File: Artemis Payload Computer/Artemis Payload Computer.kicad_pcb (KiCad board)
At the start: 2 copper layers, 11 parts, among them J1 Screw_Terminal_01x02, J2 Screw_Terminal_01x02, U1 HX711, U301 Teensy3.2, U401 FXOS8700+FXAS21002, U501 BMP280, U601 MIC39100-5.0WS

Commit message: Shit
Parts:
- removed U401: FXOS8700+FXAS21002, Artemis Payload Computer:IMU
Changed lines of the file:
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@@
     (tracks 0)
     (zones 0)
-    (modules 11)
-    (nets 67)
+    (modules 10)
+    (nets 57)
   )
   (page A4)
@@
   (net 48 "Net-(U301-Pad18)")
   (net 49 "Net-(U301-Pad17)")
-  (net 50 "Net-(U401-Pad10)")
-  (net 51 "Net-(U401-Pad9)")
-  (net 52 "Net-(U401-Pad8)")
-  (net 53 "Net-(U401-Pad7)")
-  (net 54 "Net-(U401-Pad6)")
-  (net 55 "Net-(U401-Pad5)")
-  (net 56 "Net-(U401-Pad4)")
-  (net 57 "Net-(U401-Pad3)")
-  (net 58 "Net-(U401-Pad2)")
-  (net 59 "Net-(U401-Pad1)")
-  (net 60 "Net-(U501-Pad7)")
-  (net 61 "Net-(U501-Pad6)")
-  (net 62 "Net-(U501-Pad5)")
-  (net 63 "Net-(U501-Pad4)")
-  (net 64 "Net-(U501-Pad3)")
-  (net 65 "Net-(U501-Pad2)")
-  (net 66 "Net-(U501-Pad1)")
+  (net 50 "Net-(U501-Pad7)")
+  (net 51 "Net-(U501-Pad6)")
+  (net 52 "Net-(U501-Pad5)")
+  (net 53 "Net-(U501-Pad4)")
+  (net 54 "Net-(U501-Pad3)")
+  (net 55 "Net-(U501-Pad2)")
+  (net 56 "Net-(U501-Pad1)")
   (net_class Default "This is the default net class."
     (clearance 0.2)
@@
     (add_net "Net-(U301-Pad8)")
     (add_net "Net-(U301-Pad9)")
-    (add_net "Net-(U401-Pad1)")
-    (add_net "Net-(U401-Pad10)")
-    (add_net "Net-(U401-Pad2)")
-    (add_net "Net-(U401-Pad3)")
-    (add_net "Net-(U401-Pad4)")
-    (add_net "Net-(U401-Pad5)")
-    (add_net "Net-(U401-Pad6)")
-    (add_net "Net-(U401-Pad7)")
-    (add_net "Net-(U401-Pad8)")
-    (add_net "Net-(U401-Pad9)")
     (add_net "Net-(U501-Pad1)")
     (add_net "Net-(U501-Pad2)")
@@
     (fp_line (start 16.24 2) (end -1 2) (layer F.SilkS) (width 0.12))
     (pad 7 thru_hole circle (at 15.24 0) (size 1.75 1.75) (drill 1.15) (layers *.Cu *.Mask)
-      (net 60 "Net-(U501-Pad7)"))
+      (net 50 "Net-(U501-Pad7)"))
     (pad 6 thru_hole circle (at 12.7 0) (size 1.75 1.75) (drill 1.15) (layers *.Cu *.Mask)
-      (net 61 "Net-(U501-Pad6)"))
+      (net 51 "Net-(U501-Pad6)"))
     (pad 5 thru_hole circle (at 10.16 0) (size 1.75 1.75) (drill 1.15) (layers *.Cu *.Mask)
-      (net 62 "Net-(U501-Pad5)"))
+      (net 52 "Net-(U501-Pad5)"))
     (pad 4 thru_hole circle (at 7.62 0) (size 1.75 1.75) (drill 1.15) (layers *.Cu *.Mask)
-      (net 63 "Net-(U501-Pad4)"))
+      (net 53 "Net-(U501-Pad4)"))
     (pad 3 thru_hole circle (at 5.08 0) (size 1.75 1.75) (drill 1.15) (layers *.Cu *.Mask)
-      (net 64 "Net-(U501-Pad3)"))
+      (net 54 "Net-(U501-Pad3)"))
     (pad 2 thru_hole circle (at 2.54 0) (size 1.75 1.75) (drill 1.15) (layers *.Cu *.Mask)
-      (net 65 "Net-(U501-Pad2)"))
+      (net 55 "Net-(U501-Pad2)"))
     (pad 1 thru_hole circle (at 0 0) (size 1.75 1.75) (drill 1.15) (layers *.Cu *.Mask)
-      (net 66 "Net-(U501-Pad1)"))
-  )
-  (module "Artemis Payload Computer:IMU" (layer F.Cu)
-    (at 186.971 75.897)
-    (fp_text reference U401 (at 6.3 -12.05) (layer F.SilkS)
-      (effects (font (size 1 1) (thickness 0.15)))
-    )
-    (fp_text value FXOS8700+FXAS21002 (at 6.07 -13.55) (layer F.Fab)
-      (effects (font (size 1 1) (thickness 0.15)))
-    )
-    (fp_text user IMU (at 6.3 -6.69) (layer F.SilkS)
-      (effects (font (size 2 2) (thickness 0.3)))
-    )
-    (fp_line (start -7.61 2.54) (end 20.31 2.54) (layer F.SilkS) (width 0.12))
-    (fp_line (start 20.31 2.54) (end 20.31 -17.78) (layer F.SilkS) (width 0.12))
-    (fp_line (start -7.61 -17.78) (end 20.31 -17.78) (layer F.SilkS) (width 0.12))
-    (fp_line (start -7.61 2.54) (end -7.61 -17.78) (layer F.SilkS) (width 0.12))
-    (pad 10 thru_hole circle (at 10.16 -15.24) (size 1.75 1.75) (drill 1.15) (layers *.Cu *.Mask)
-      (net 50 "Net-(U401-Pad10)"))
-    (pad 9 thru_hole circle (at 7.62 -15.24) (size 1.75 1.75) (drill 1.15) (layers *.Cu *.Mask)
-      (net 51 "Net-(U401-Pad9)"))
-    (pad 8 thru_hole circle (at 5.08 -15.24) (size 1.75 1.75) (drill 1.15) (layers *.Cu *.Mask)
-      (net 52 "Net-(U401-Pad8)"))
-    (pad 7 thru_hole circle (at 2.54 -15.24) (size 1.75 1.75) (drill 1.15) (layers *.Cu *.Mask)
-      (net 53 "Net-(U401-Pad7)"))
-    (pad 6 thru_hole circle (at 12.7 0) (size 1.75 1.75) (drill 1.15) (layers *.Cu *.Mask)
-      (net 54 "Net-(U401-Pad6)"))
-    (pad 5 thru_hole circle (at 10.16 0) (size 1.75 1.75) (drill 1.15) (layers *.Cu *.Mask)
-      (net 55 "Net-(U401-Pad5)"))
-    (pad 4 thru_hole circle (at 7.62 0) (size 1.75 1.75) (drill 1.15) (layers *.Cu *.Mask)
-      (net 56 "Net-(U401-Pad4)"))
-    (pad 3 thru_hole circle (at 5.08 0) (size 1.75 1.75) (drill 1.15) (layers *.Cu *.Mask)
-      (net 57 "Net-(U401-Pad3)"))
-    (pad 2 thru_hole circle (at 2.54 0) (size 1.75 1.75) (drill 1.15) (layers *.Cu *.Mask)
-      (net 58 "Net-(U401-Pad2)"))
-    (pad 1 thru_hole circle (at 0 0) (size 1.75 1.75) (drill 1.15) (layers *.Cu *.Mask)
-      (net 59 "Net-(U401-Pad1)"))
+      (net 56 "Net-(U501-Pad1)"))
   )
   (module "Artemis Payload Computer:Teensy30_31_32_LC" (layer F.Cu)

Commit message: ready for testing...
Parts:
- added J601: Connector_Screw_Terminal_01x02, TerminalBlock:TerminalBlock_bornier-2_P5.08mm, F.Cu at (211.4, 115.4)
- added U401: ICM-20948, Artemis Payload Computer:ICM-20948, F.Cu at (182.3, 114.8)
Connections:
- net Net-(U301-Pad25) renamed /Teensy3.2/SDA0
- net Net-(U301-Pad26) renamed /Teensy3.2/SCL0
- net Net-(U501-Pad4) renamed /BMP280/SCL0
- net Net-(U501-Pad6) renamed /BMP280/SDA0
- U301 pad 1: Net-(U301-Pad1) -> GND
- U301 pad 17: Net-(U301-Pad17) -> GND
- U301 pad 32: Net-(U301-Pad32) -> GND
- U501 pad 1: Net-(U501-Pad1) -> +5V
- U501 pad 3: Net-(U501-Pad3) -> GND

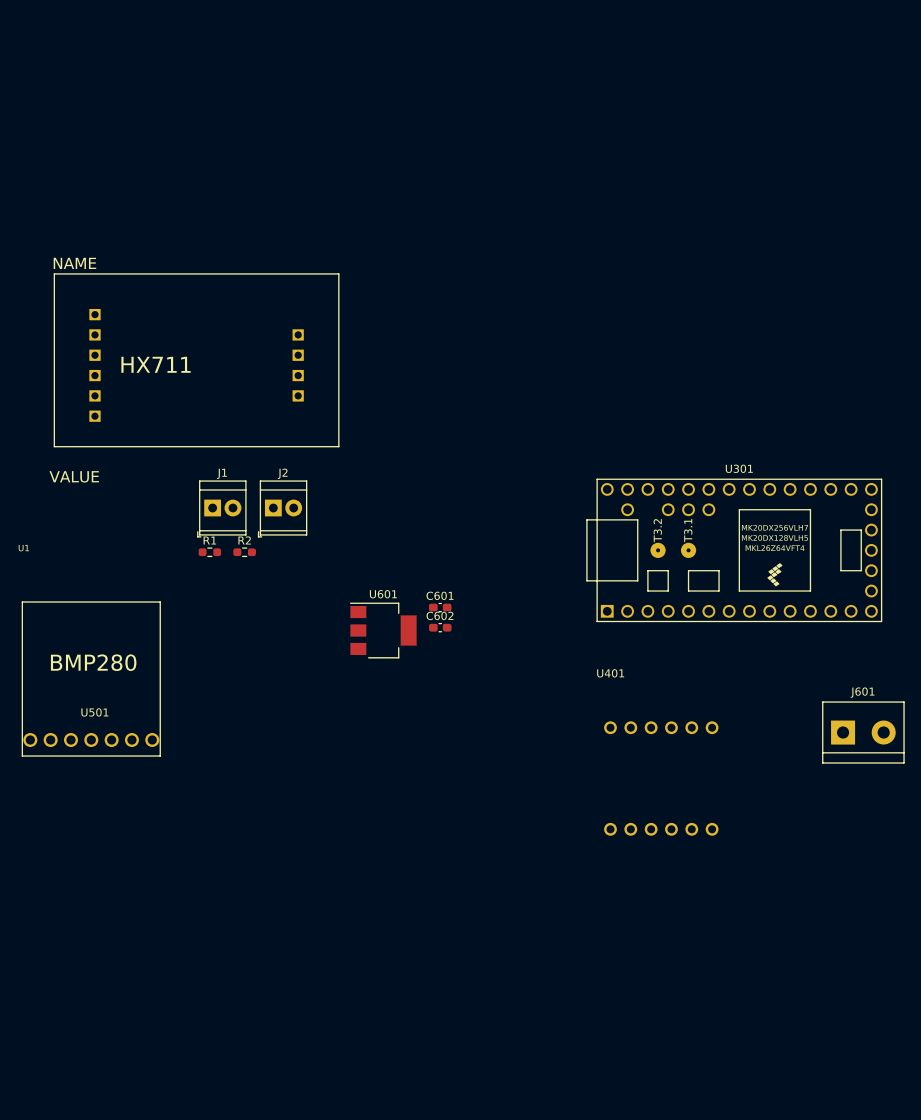
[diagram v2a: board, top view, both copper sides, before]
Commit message: Continued work on SD card. Starting PCB layout.
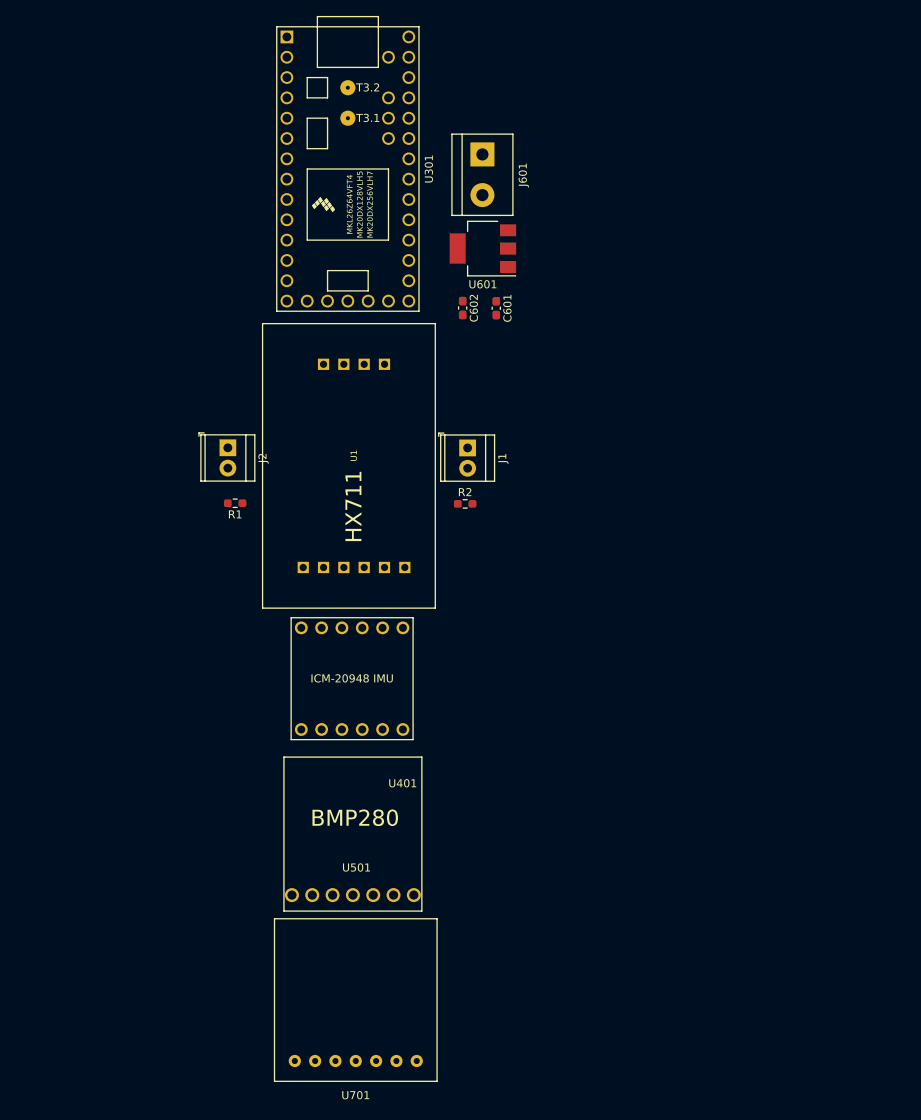
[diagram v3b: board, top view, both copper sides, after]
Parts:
- added U701: MicroSD_Breakout_Sparkfun, Artemis Payload Computer:MicroSD_Breakout, F.Cu at (158.1, 156.5)
- U1: footprint .pretty:HX711 -> Artemis Payload Computer:HX711
- moved J601 85.2 mm to (166.3, 43.2), turned to 270 degrees
- moved U301 68.3 mm to (149.5, 45.0), turned to 270 degrees
- moved U1 65.1 mm to (173.1, 103.7), turned to 90 degrees
- moved U601 49.3 mm to (166.4, 55.0), turned to 180 degrees
- moved C602 40.1 mm to (163.8, 62.4), turned to 270 degrees
- moved C601 38.1 mm to (168.0, 62.4), turned to 270 degrees
- moved U501 38.0 mm to (142.5, 135.8)
- moved J1 32.7 mm to (164.5, 79.9), turned to 270 degrees
- moved R2 28.2 mm to (164.2, 86.9)
- moved U401 26.0 mm to (156.4, 115.1), turned to 180 degrees
- moved J2 9.43 mm to (134.5, 79.8), turned to 270 degrees
- moved R1 6.89 mm to (135.4, 86.8), turned to 180 degrees

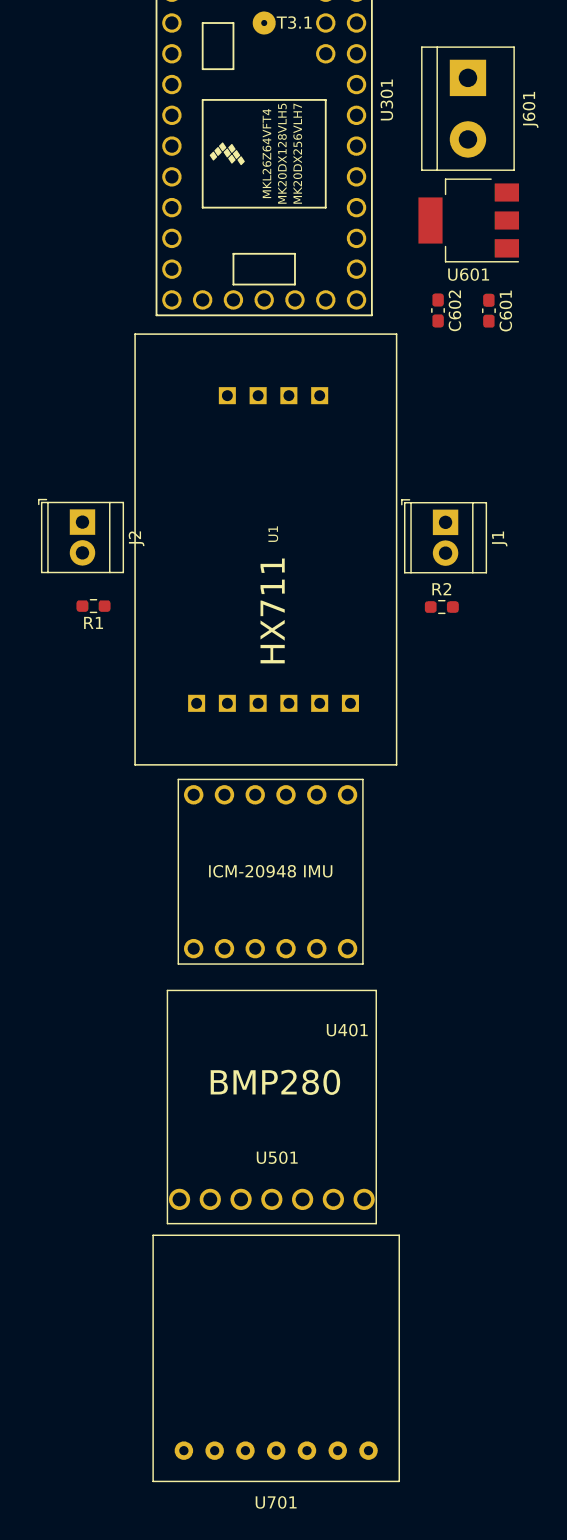
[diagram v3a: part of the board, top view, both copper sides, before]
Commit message: started tracing... they are bad
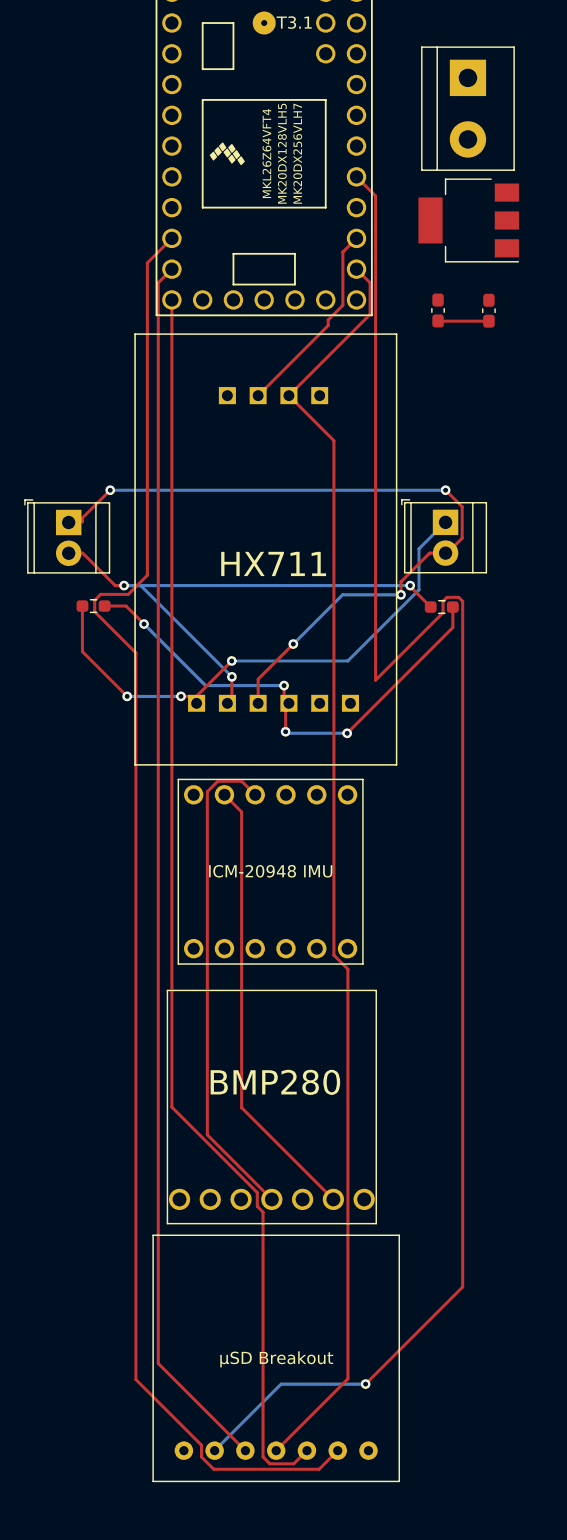
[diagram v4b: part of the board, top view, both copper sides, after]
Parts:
- moved J2 1.14 mm to (133.3, 79.9)
- renumbered U301 to U2
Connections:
- U1 pad DT: /WS STRAIN GAUGE/DT -> /DT
- U1 pad SCK: /WS STRAIN GAUGE/SCK -> /SCK
- U2 pad 12: Net-(U301-Pad12) -> /CS
- U2 pad 13: Net-(U301-Pad13) -> /DO
- U2 pad 14: Net-(U301-Pad14) -> /DI
- U2 pad 21: Net-(U301-Pad21) -> /SCK
- U2 pad 22: Net-(U301-Pad22) -> /DT
- U2 pad 24: Net-(U301-Pad24) -> /CD
- U2 pad 25: /Teensy3.2/SDA0 -> /SDA0
- U2 pad 26: /Teensy3.2/SCL0 -> /SCL0
- U2 pad 33: Net-(U301-Pad33) -> +5V
- U401 pad 4: /IMU/SCL0 -> /SCL0
- U401 pad 5: /IMU/SDA0 -> /SDA0
- U501 pad 4: /BMP280/SCL0 -> /SCL0
- U501 pad 6: /BMP280/SDA0 -> /SDA0
- U701 pad 2: /SD_card/CS -> /CS
- U701 pad 3: /SD_card/DI -> /DI
- U701 pad 4: /SD_card/SCK -> /SCK
- U701 pad 5: /SD_card/DO -> /DO
- U701 pad 6: /SD_card/CD -> /CD
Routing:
- net /CD: track 0.00 -> 135.6 mm, vias 0 -> 1
- net /CS: track 0.00 -> 120.5 mm
- net /SCK: track 0.00 -> 105.2 mm
- net /DI: track 0.00 -> 102.9 mm
- net /DO: track 0.00 -> 101.0 mm
- net Net-(J1-Pad2): track 0.00 -> 60.1 mm, vias 0 -> 4
- net Net-(J2-Pad2): track 0.00 -> 45.0 mm, vias 0 -> 3
- net Net-(J1-Pad1): track 0.00 -> 44.0 mm, vias 0 -> 3
- net Net-(R1-Pad1): track 0.00 -> 40.8 mm, vias 0 -> 4
- net /SCL0: track 0.00 -> 40.6 mm
- net /SDA0: track 0.00 -> 37.1 mm
- net /DT: track 0.00 -> 16.3 mm
- net GND: track 0.00 -> 4.21 mm

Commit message: redid layout
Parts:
- moved U701 76.8 mm to (136.1, 82.9)
- moved U501 55.2 mm to (159.7, 83.3)
- moved U1 42.7 mm to (151.8, 66.7)
- moved R1 40.3 mm to (168.4, 63.7)
- moved J2 40.3 mm to (166.3, 56.8)
- moved J1 37.4 mm to (175.9, 44.3)
- moved R2 37.4 mm to (175.6, 51.3)
- moved U401 34.9 mm to (155.7, 80.2)
- moved J601 13.2 mm to (166.2, 30.0)
- moved C601 10.8 mm to (167.9, 51.6)
- moved C602 10.8 mm to (163.7, 51.6)
- moved U601 10.7 mm to (166.1, 44.3)
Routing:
- net /CD: track 135.6 -> 0.00 mm, vias 1 -> 0
- net /CS: track 120.5 -> 29.9 mm
- net /DI: track 102.9 -> 32.3 mm
- net /DO: track 101.0 -> 32.9 mm, vias 0 -> 1
- net /SDA0: track 37.1 -> 70.6 mm
- net Net-(J1-Pad1): track 44.0 -> 77.1 mm, vias 3 -> 2
- net /SCL0: track 40.6 -> 66.8 mm
- net Net-(R1-Pad1): track 40.8 -> 62.2 mm, vias 4 -> 2
- net +BATT: track 0.00 -> 19.7 mm
- net /DT: track 16.3 -> 0.00 mm
- net /SCK: track 105.2 -> 91.3 mm, vias 0 -> 2
- net Net-(J2-Pad2): track 45.0 -> 56.7 mm, vias 3 -> 2
- net Net-(J1-Pad2): track 60.1 -> 54.8 mm, vias 4 -> 2

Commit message: ready for review
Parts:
- moved J1 58.2 mm to (125.0, 72.5)
- moved R2 51.3 mm to (132.5, 79.1), turned to 90 degrees
- moved J2 48.7 mm to (125.0, 82.5), turned to 90 degrees
- moved R1 37.0 mm to (132.5, 72.5), turned to 90 degrees
- moved U401 34.6 mm to (179.5, 55.0), turned to 270 degrees
- moved U701 24.3 mm to (160.0, 87.5)
- moved U501 23.2 mm to (180.6, 73.2), turned to 180 degrees
- moved C602 13.7 mm to (176.0, 45.5)
- moved J601 13.0 mm to (175.1, 39.5), turned to 90 degrees
- moved C601 8.48 mm to (176.0, 49.0), turned to 90 degrees
- moved U1 6.65 mm to (155.0, 72.5)
- moved U2 5.84 mm to (152.5, 50.0)
- moved U601 5.09 mm to (170.0, 47.5)
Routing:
- net /CD: track 0.00 -> 51.5 mm
- net Net-(J1-Pad1): track 77.1 -> 28.8 mm, vias 2 -> 0
- net /DT: track 0.00 -> 47.4 mm
- net /SDA0: track 70.6 -> 23.5 mm
- net Net-(R1-Pad1): track 62.2 -> 15.2 mm, vias 2 -> 0
- net /SCL0: track 66.8 -> 27.8 mm
- net GND: track 4.21 -> 41.0 mm
- net Net-(J2-Pad2): track 56.7 -> 23.6 mm, vias 2 -> 0
- net Net-(J1-Pad2): track 54.8 -> 29.8 mm, vias 2 -> 0
- net +5V: track 0.00 -> 15.5 mm
- net /SCK: track 91.3 -> 79.2 mm, vias 2 -> 0
- net /DI: track 32.3 -> 25.1 mm
- net /DO: track 32.9 -> 26.5 mm, vias 1 -> 0
- net Net-(U2-Pad52): track 0.00 -> 3.81 mm
- net /CS: track 29.9 -> 31.3 mm
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- added copper zone on B.Cu, net +5V
- added copper zone on F.Cu, net GND
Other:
- board outline added: 64.7 x 61 mm

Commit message: Minor Changes. Approved for ordering
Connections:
- U601 pad 4: (no net) -> GND
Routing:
- net /CD: track 51.5 -> 37.9 mm, vias 0 -> 2
- net +5V: track 15.5 -> 6.56 mm, vias 0 -> 1
- net /SCK: track 79.2 -> 72.2 mm, vias 0 -> 1
- net Net-(J1-Pad2): track 29.8 -> 24.4 mm, vias 0 -> 1
- net Net-(J2-Pad2): track 23.6 -> 25.2 mm
- net /DO: track 26.5 -> 27.2 mm

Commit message: updated resistor footprint. still ready for ordering
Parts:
- R1, R2: footprint Resistor_SMD:R_0603_1608Metric_Pad0.98x0.95mm_HandSolder -> Resistor_THT:R_Axial_DIN0309_L9.0mm_D3.2mm_P12.70mm_Horizontal
- moved R2 9.00 mm to (139.5, 84.8)
- moved R1 2.29 mm to (134.8, 72.0), turned to 270 degrees
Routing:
- net Net-(J2-Pad2): track 25.2 -> 32.7 mm
- net Net-(J1-Pad1): track 28.8 -> 35.7 mm
- net Net-(R1-Pad1): track 15.2 -> 13.7 mm
